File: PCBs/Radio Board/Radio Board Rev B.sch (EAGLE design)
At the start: 4 parts

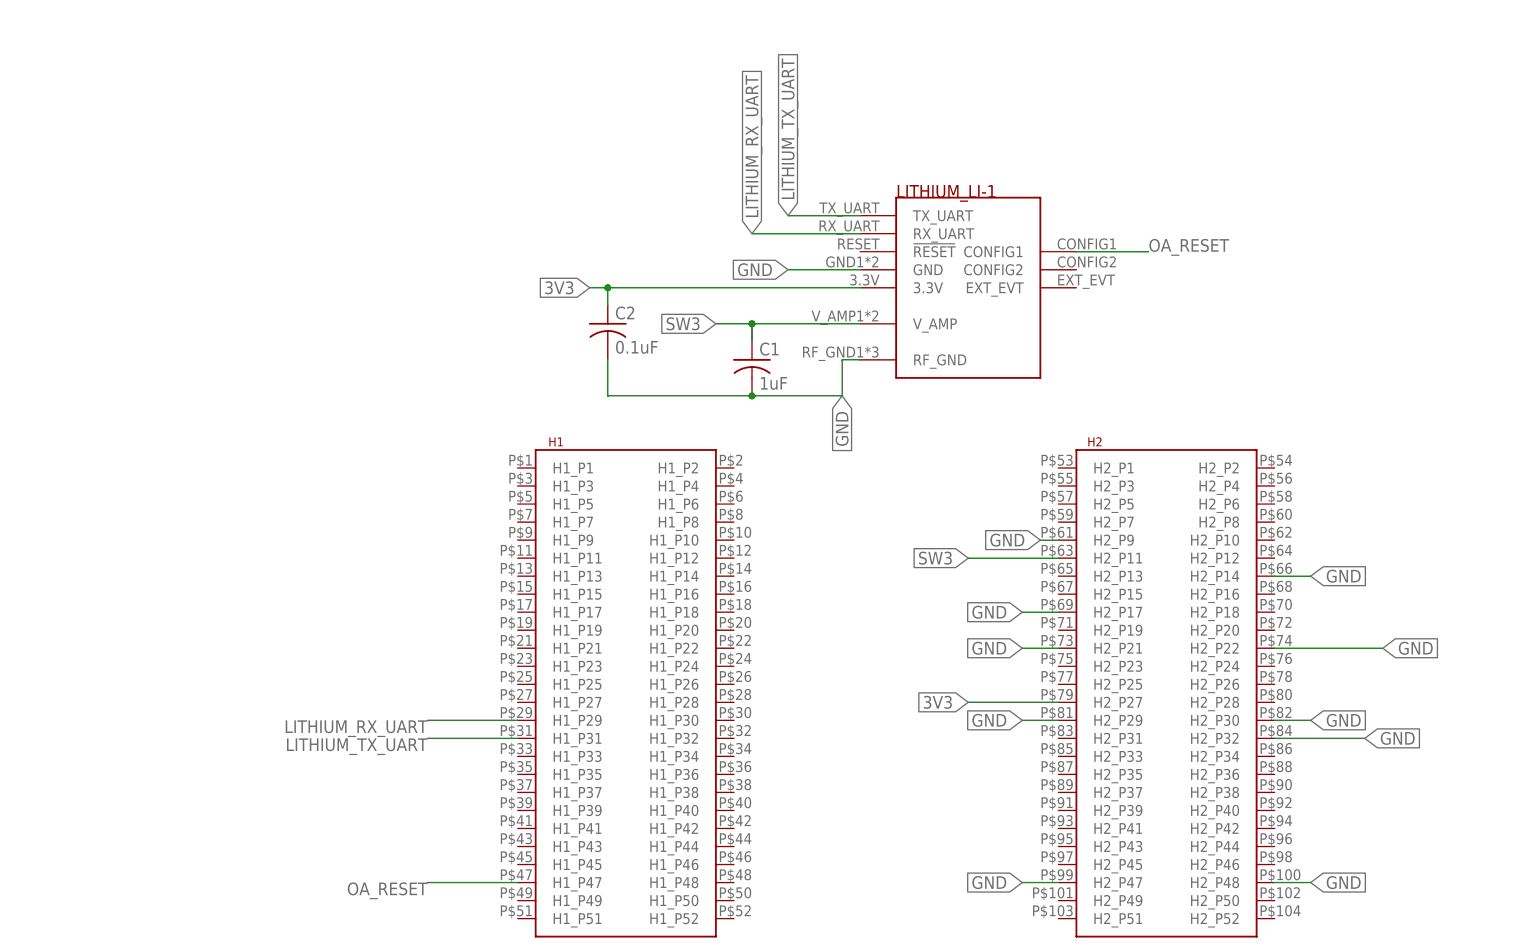
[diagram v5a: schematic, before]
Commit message: Update radio board to use new library
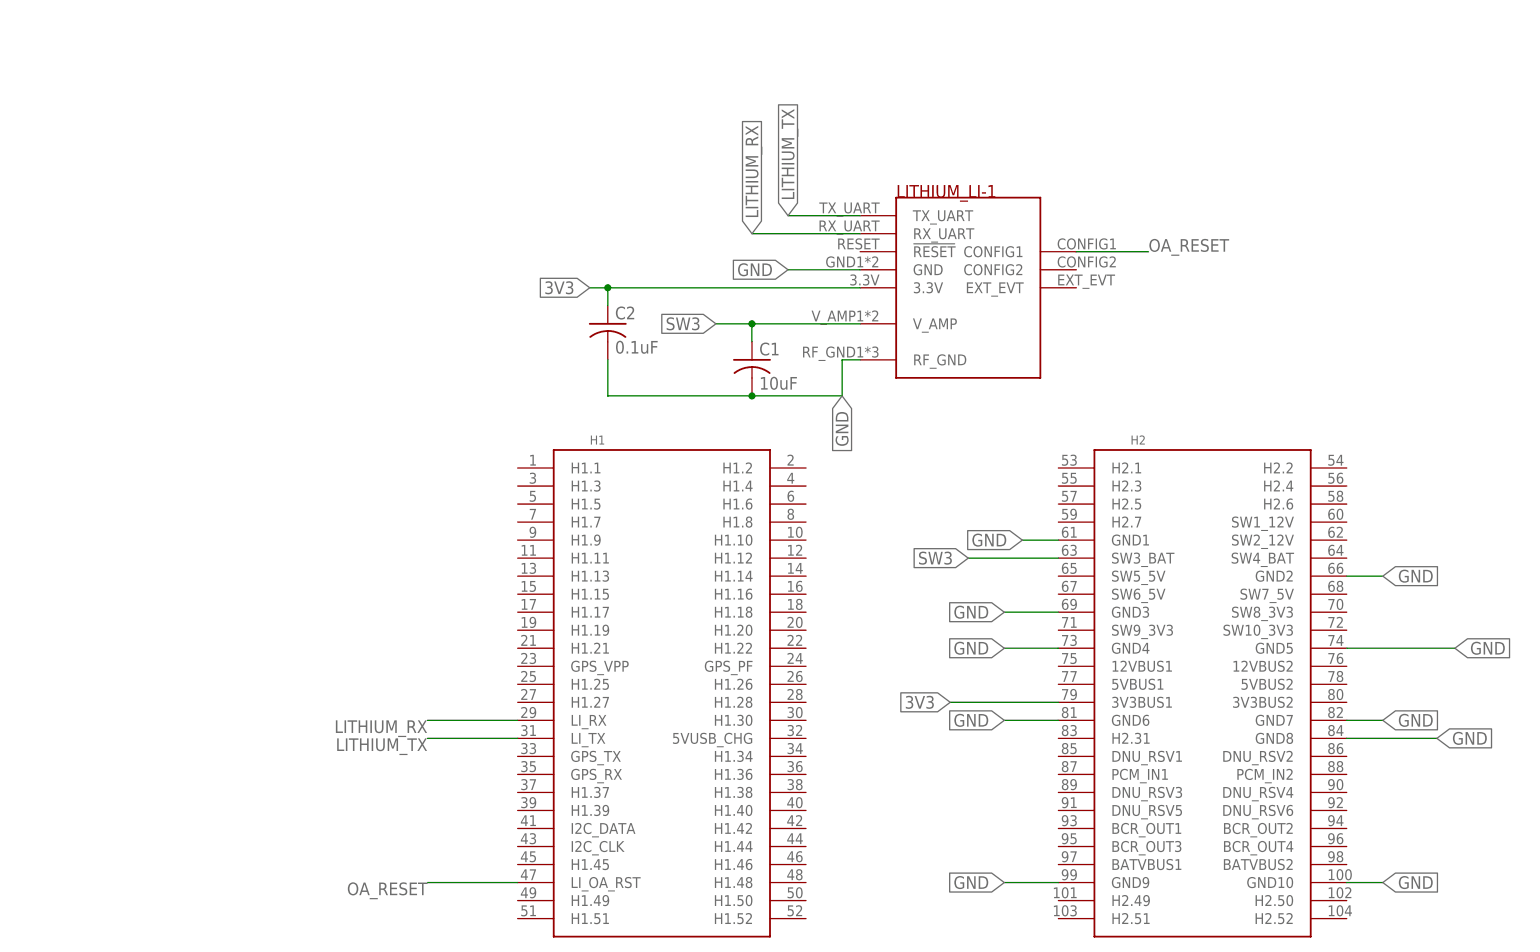
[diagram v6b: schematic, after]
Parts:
- C1: value 1uF -> 10uF
- U$1: value LITHIUM -> LI-1; device Cubesat:LITHIUM -> Cubesat:LI-1
- U$2: value PC104 -> PC104_BOARD; device Cubesat:PC104 -> Cubesat:PC104_BOARD
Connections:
- removed net LITHIUM_RX_UART: U$1.RX_UART, U$2.H1_P29
- removed net LITHIUM_TX_UART: U$1.TX_UART, U$2.H1_P31
- new net LITHIUM_RX: U$1.RX_UART, U$2.LI_RX
- new net LITHIUM_TX: U$1.TX_UART, U$2.LI_TX
- net 3V3: now also U$2.3V3BUS1; no longer U$2.H2_P27
- net GND: now also U$2.GND1, U$2.GND10, U$2.GND2, U$2.GND3, U$2.GND4, U$2.GND5, U$2.GND6, U$2.GND7, U$2.GND8, U$2.GND9; no longer U$2.H2_P14, U$2.H2_P17, U$2.H2_P21, U$2.H2_P22, U$2.H2_P29, U$2.H2_P30, U$2.H2_P32, U$2.H2_P47, U$2.H2_P48, U$2.H2_P9
- net OA_RESET: now also U$2.LI_OA_RST; no longer U$2.H1_P47
- net SW3: now also U$2.SW3_BAT; no longer U$2.H2_P11
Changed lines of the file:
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@@
 <?xml version="1.0" encoding="utf-8"?>
 <!DOCTYPE eagle SYSTEM "eagle.dtd">
-<eagle version="9.1.0">
+<eagle version="9.1.1">
 <drawing>
 <settings>
@@
 </classes>
 <parts>
-<part name="U$1" library="Cubesat" deviceset="LITHIUM" device=""/>
-<part name="U$2" library="Cubesat" deviceset="PC104" device=""/>
-<part name="C1" library="resistor" library_urn="urn:adsk.eagle:library:348" deviceset="C-US" device="C0805" package3d_urn="urn:adsk.eagle:package:26137/1" value="1uF"/>
+<part name="C1" library="resistor" library_urn="urn:adsk.eagle:library:348" deviceset="C-US" device="C0805" package3d_urn="urn:adsk.eagle:package:26137/1" value="10uF"/>
 <part name="C2" library="resistor" library_urn="urn:adsk.eagle:library:348" deviceset="C-US" device="C0805" package3d_urn="urn:adsk.eagle:package:26137/1" value="0.1uF"/>
+<part name="U$1" library="Cubesat" deviceset="LI-1" device=""/>
+<part name="U$2" library="Cubesat" deviceset="PC104_BOARD" device=""/>
 </parts>
 <sheets>
@@
 </plain>
 <instances>
-<instance part="U$1" gate="G$1" x="76.2" y="78.74"/>
-<instance part="U$2" gate="G$1" x="25.4" y="0"/>
 <instance part="C1" gate="G$1" x="55.88" y="81.28"/>
 <instance part="C2" gate="G$1" x="35.56" y="86.36"/>
+<instance part="U$1" gate="G$1" x="76.2" y="78.74"/>
+<instance part="U$2" gate="A" x="22.86" y="66.04"/>
 </instances>
 <busses>
@@
 <net name="GND" class="0">
 <segment>
-<pinref part="U$2" gate="G$1" pin="H2_P9"/>
-<wire x1="99.06" y1="55.88" x2="96.52" y2="55.88" width="0.1524" layer="91"/>
-<label x="96.52" y="55.88" size="1.778" layer="95" rot="R180" xref="yes"/>
-</segment>
-<segment>
-<pinref part="U$2" gate="G$1" pin="H2_P22"/>
-<wire x1="129.54" y1="40.64" x2="144.78" y2="40.64" width="0.1524" layer="91"/>
-<label x="144.78" y="40.64" size="1.778" layer="95" xref="yes"/>
-</segment>
-<segment>
-<pinref part="U$1" gate="G$1" pin="GND"/>
+<wire x1="99.06" y1="55.88" x2="93.98" y2="55.88" width="0.1524" layer="91"/>
+<label x="93.98" y="55.88" size="1.778" layer="95" rot="R180" xref="yes"/>
+<pinref part="U$2" gate="A" pin="GND1"/>
+</segment>
+<segment>
+<wire x1="139.7" y1="40.64" x2="154.94" y2="40.64" width="0.1524" layer="91"/>
+<label x="154.94" y="40.64" size="1.778" layer="95" xref="yes"/>
+<pinref part="U$2" gate="A" pin="GND5"/>
+</segment>
+<segment>
 <wire x1="71.12" y1="93.98" x2="60.96" y2="93.98" width="0.1524" layer="91"/>
 <label x="60.96" y="93.98" size="1.778" layer="95" rot="R180" xref="yes"/>
-</segment>
-<segment>
-<pinref part="U$2" gate="G$1" pin="H2_P21"/>
-<wire x1="99.06" y1="40.64" x2="93.98" y2="40.64" width="0.1524" layer="91"/>
-<label x="93.98" y="40.64" size="1.778" layer="95" rot="R180" xref="yes"/>
-</segment>
-<segment>
-<pinref part="U$2" gate="G$1" pin="H2_P14"/>
-<wire x1="129.54" y1="50.8" x2="134.62" y2="50.8" width="0.1524" layer="91"/>
-<label x="134.62" y="50.8" size="1.778" layer="95" xref="yes"/>
-</segment>
-<segment>
-<pinref part="U$2" gate="G$1" pin="H2_P17"/>
-<wire x1="99.06" y1="45.72" x2="93.98" y2="45.72" width="0.1524" layer="91"/>
-<label x="93.98" y="45.72" size="1.778" layer="95" rot="R180" xref="yes"/>
-</segment>
-<segment>
-<pinref part="U$2" gate="G$1" pin="H2_P29"/>
-<wire x1="99.06" y1="30.48" x2="93.98" y2="30.48" width="0.1524" layer="91"/>
-<label x="93.98" y="30.48" size="1.778" layer="95" rot="R180" xref="yes"/>
-</segment>
-<segment>
-<pinref part="U$2" gate="G$1" pin="H2_P47"/>
-<wire x1="99.06" y1="7.62" x2="93.98" y2="7.62" width="0.1524" layer="91"/>
-<label x="93.98" y="7.62" size="1.778" layer="95" rot="R180" xref="yes"/>
-</segment>
-<segment>
-<pinref part="U$2" gate="G$1" pin="H2_P30"/>
-<wire x1="129.54" y1="30.48" x2="134.62" y2="30.48" width="0.1524" layer="91"/>
-<label x="134.62" y="30.48" size="1.778" layer="95" xref="yes"/>
-</segment>
-<segment>
-<pinref part="U$2" gate="G$1" pin="H2_P32"/>
-<wire x1="129.54" y1="27.94" x2="142.24" y2="27.94" width="0.1524" layer="91"/>
-<label x="142.24" y="27.94" size="1.778" layer="95" xref="yes"/>
-</segment>
-<segment>
-<pinref part="U$2" gate="G$1" pin="H2_P48"/>
-<wire x1="129.54" y1="7.62" x2="134.62" y2="7.62" width="0.1524" layer="91"/>
-<label x="134.62" y="7.62" size="1.778" layer="95" xref="yes"/>
+<pinref part="U$1" gate="G$1" pin="GND"/>
+</segment>
+<segment>
+<wire x1="99.06" y1="40.64" x2="91.44" y2="40.64" width="0.1524" layer="91"/>
+<label x="91.44" y="40.64" size="1.778" layer="95" rot="R180" xref="yes"/>
+<pinref part="U$2" gate="A" pin="GND4"/>
+</segment>
+<segment>
+<wire x1="139.7" y1="50.8" x2="144.78" y2="50.8" width="0.1524" layer="91"/>
+<label x="144.78" y="50.8" size="1.778" layer="95" xref="yes"/>
+<pinref part="U$2" gate="A" pin="GND2"/>
+</segment>
+<segment>
+<wire x1="99.06" y1="45.72" x2="91.44" y2="45.72" width="0.1524" layer="91"/>
+<label x="91.44" y="45.72" size="1.778" layer="95" rot="R180" xref="yes"/>
+<pinref part="U$2" gate="A" pin="GND3"/>
+</segment>
+<segment>
+<wire x1="99.06" y1="30.48" x2="91.44" y2="30.48" width="0.1524" layer="91"/>
+<label x="91.44" y="30.48" size="1.778" layer="95" rot="R180" xref="yes"/>
+<pinref part="U$2" gate="A" pin="GND6"/>
+</segment>
+<segment>
+<wire x1="99.06" y1="7.62" x2="91.44" y2="7.62" width="0.1524" layer="91"/>
+<label x="91.44" y="7.62" size="1.778" layer="95" rot="R180" xref="yes"/>
+<pinref part="U$2" gate="A" pin="GND9"/>
+</segment>
+<segment>
+<wire x1="139.7" y1="30.48" x2="144.78" y2="30.48" width="0.1524" layer="91"/>
+<label x="144.78" y="30.48" size="1.778" layer="95" xref="yes"/>
+<pinref part="U$2" gate="A" pin="GND7"/>
+</segment>
+<segment>
+<wire x1="139.7" y1="27.94" x2="152.4" y2="27.94" width="0.1524" layer="91"/>
+<label x="152.4" y="27.94" size="1.778" layer="95" xref="yes"/>
+<pinref part="U$2" gate="A" pin="GND8"/>
+</segment>
+<segment>
+<wire x1="139.7" y1="7.62" x2="144.78" y2="7.62" width="0.1524" layer="91"/>
+<label x="144.78" y="7.62" size="1.778" layer="95" xref="yes"/>
+<pinref part="U$2" gate="A" pin="GND10"/>
 </segment>
 <segment>
@@
 <junction x="55.88" y="76.2"/>
 <wire x1="68.58" y1="76.2" x2="68.58" y2="81.28" width="0.1524" layer="91"/>
-<pinref part="U$1" gate="G$1" pin="RF_GND"/>
 <wire x1="68.58" y1="81.28" x2="71.12" y2="81.28" width="0.1524" layer="91"/>
 <label x="68.58" y="76.2" size="1.778" layer="95" rot="R270" xref="yes"/>
+<pinref part="U$1" gate="G$1" pin="RF_GND"/>
 </segment>
 </net>
 <net name="SW3" class="0">
 <segment>
-<pinref part="U$2" gate="G$1" pin="H2_P11"/>
 <wire x1="99.06" y1="53.34" x2="86.36" y2="53.34" width="0.1524" layer="91"/>
 <label x="86.36" y="53.34" size="1.778" layer="95" rot="R180" xref="yes"/>
-</segment>
-<segment>
-<pinref part="U$1" gate="G$1" pin="V_AMP"/>
+<pinref part="U$2" gate="A" pin="SW3_BAT"/>
+</segment>
+<segment>
 <wire x1="71.12" y1="86.36" x2="55.88" y2="86.36" width="0.1524" layer="91"/>
 <label x="50.8" y="86.36" size="1.778" layer="95" rot="R180" xref="yes"/>
@@
 <wire x1="55.88" y1="86.36" x2="55.88" y2="83.82" width="0.1524" layer="91"/>
 <junction x="55.88" y="86.36"/>
-</segment>
-</net>
-<net name="LITHIUM_TX_UART" class="0">
-<segment>
-<pinref part="U$1" gate="G$1" pin="TX_UART"/>
+<pinref part="U$1" gate="G$1" pin="V_AMP"/>
+</segment>
+</net>
+<net name="LITHIUM_TX" class="0">
+<segment>
 <wire x1="71.12" y1="101.6" x2="60.96" y2="101.6" width="0.1524" layer="91"/>
 <label x="60.96" y="101.6" size="1.778" layer="95" rot="R90" xref="yes"/>
-</segment>
-<segment>
-<pinref part="U$2" gate="G$1" pin="H1_P31"/>
+<pinref part="U$1" gate="G$1" pin="TX_UART"/>
+</segment>
+<segment>
 <wire x1="22.86" y1="27.94" x2="10.16" y2="27.94" width="0.1524" layer="91"/>
 <label x="10.16" y="27.94" size="1.778" layer="95" rot="R180"/>
-</segment>
-</net>
-<net name="LITHIUM_RX_UART" class="0">
-<segment>
-<pinref part="U$1" gate="G$1" pin="RX_UART"/>
+<pinref part="U$2" gate="A" pin="LI_TX"/>
+</segment>
+</net>
+<net name="LITHIUM_RX" class="0">
+<segment>
 <wire x1="71.12" y1="99.06" x2="55.88" y2="99.06" width="0.1524" layer="91"/>
 <label x="55.88" y="99.06" size="1.778" layer="95" rot="R90" xref="yes"/>
-</segment>
-<segment>
-<pinref part="U$2" gate="G$1" pin="H1_P29"/>
+<pinref part="U$1" gate="G$1" pin="RX_UART"/>
+</segment>
+<segment>
 <wire x1="22.86" y1="30.48" x2="10.16" y2="30.48" width="0.1524" layer="91"/>
 <label x="10.16" y="30.48" size="1.778" layer="95" rot="R180"/>
+<pinref part="U$2" gate="A" pin="LI_RX"/>
 </segment>
 </net>
 <net name="3V3" class="0">
 <segment>
-<pinref part="U$2" gate="G$1" pin="H2_P27"/>
-<wire x1="99.06" y1="33.02" x2="86.36" y2="33.02" width="0.1524" layer="91"/>
-<label x="86.36" y="33.02" size="1.778" layer="95" rot="R180" xref="yes"/>
-</segment>
-<segment>
-<pinref part="U$1" gate="G$1" pin="3.3V"/>
+<wire x1="99.06" y1="33.02" x2="83.82" y2="33.02" width="0.1524" layer="91"/>
+<label x="83.82" y="33.02" size="1.778" layer="95" rot="R180" xref="yes"/>
+<pinref part="U$2" gate="A" pin="3V3BUS1"/>
+</segment>
+<segment>
 <wire x1="71.12" y1="91.44" x2="35.56" y2="91.44" width="0.1524" layer="91"/>
 <pinref part="C2" gate="G$1" pin="1"/>
@@
 <junction x="35.56" y="91.44"/>
 <label x="33.02" y="91.44" size="1.778" layer="95" rot="R180" xref="yes"/>
+<pinref part="U$1" gate="G$1" pin="3.3V"/>
 </segment>
 </net>
 <net name="OA_RESET" class="0">
 <segment>
-<pinref part="U$1" gate="G$1" pin="CONFIG1"/>
 <wire x1="101.6" y1="96.52" x2="111.76" y2="96.52" width="0.1524" layer="91"/>
 <label x="111.76" y="96.52" size="1.778" layer="95"/>
-</segment>
-<segment>
-<pinref part="U$2" gate="G$1" pin="H1_P47"/>
+<pinref part="U$1" gate="G$1" pin="CONFIG1"/>
+</segment>
+<segment>
 <wire x1="22.86" y1="7.62" x2="10.16" y2="7.62" width="0.1524" layer="91"/>
 <label x="10.16" y="7.62" size="1.778" layer="95" rot="R180"/>
-</segment>
-</net>
+<pinref part="U$2" gate="A" pin="LI_OA_RST"/>
+</segment>
+</net>
